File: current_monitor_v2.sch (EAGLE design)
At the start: 21 parts, among them IC1 LT1495, J1 1X2-3.5MM, J2 1X2-3.5MM, SW2 Display, T1 2N3904, T2 2N3904, U1 ARDUINO_SHIELDLABEL

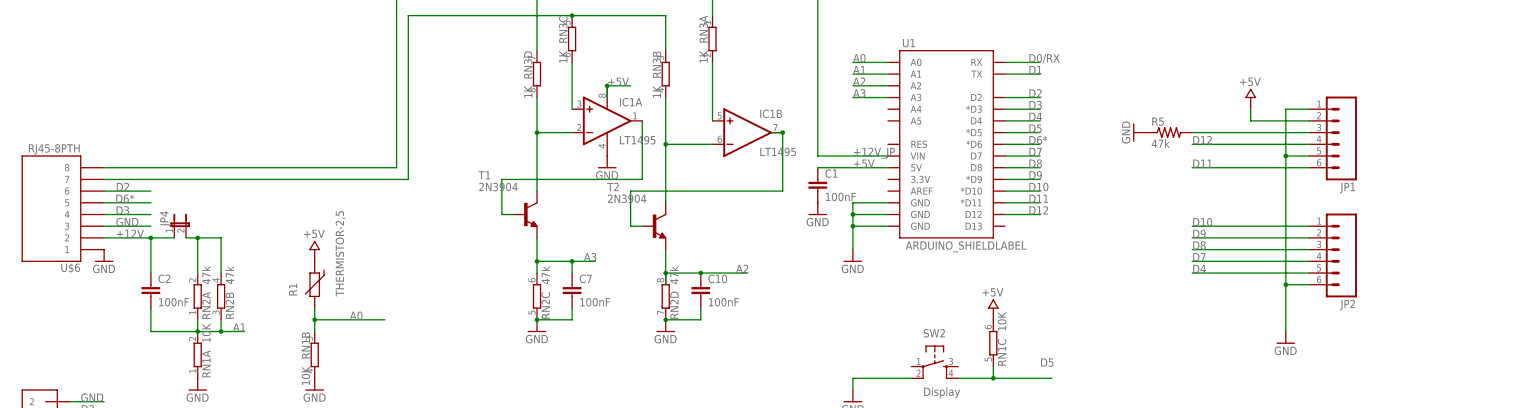
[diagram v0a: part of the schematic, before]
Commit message: changed v1.1 to v1-1 to please git, surface mount board ready to submit to osh park
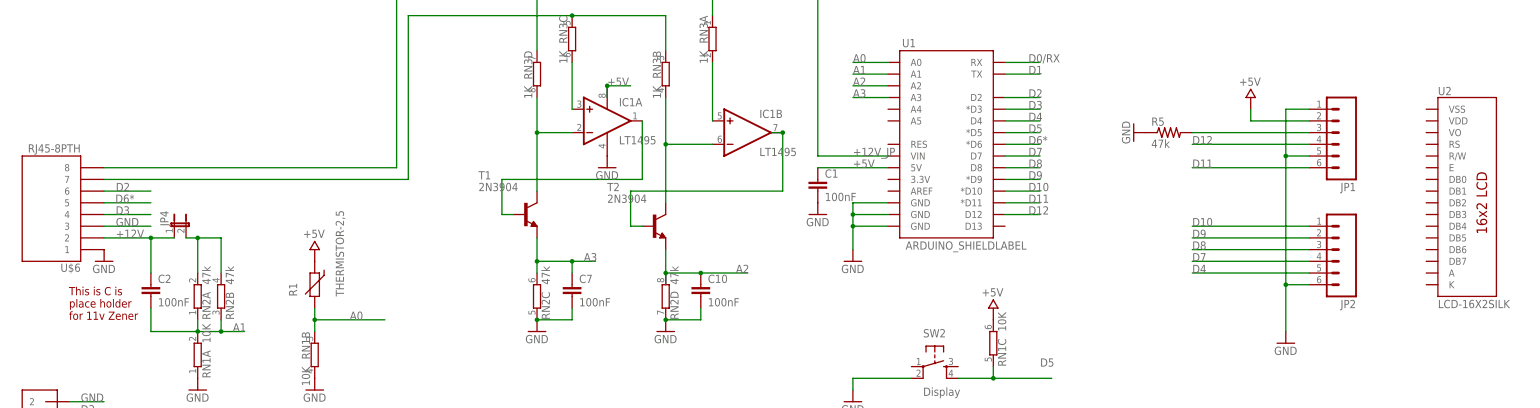
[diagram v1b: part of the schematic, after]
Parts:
- added U2: LCD-16X2SILK, SparkFun-Displays:LCD-16X2SILK
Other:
- note added: "This is C is place holder for 11v Zener"
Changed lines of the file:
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@@
 <part name="JP3" library="SparkFun-Passives" deviceset="JUMPER-2" device="PTH"/>
 <part name="JP4" library="SparkFun-Passives" deviceset="JUMPER-2" device="PTH"/>
+<part name="U2" library="SparkFun-Displays" deviceset="LCD-16X2" device="SILK"/>
 </parts>
 <sheets>
@@
 <text x="189.23" y="-58.928" size="2.54" layer="97">8</text>
 <text x="190.5" y="-68.58" size="1.778" layer="91">GJH</text>
+<text x="-106.68" y="53.34" size="1.778" layer="94">This is C is
+place holder
+for 11v Zener</text>
 </plain>
 <instances>
@@
 <instance part="JP3" gate="A" x="48.26" y="132.08"/>
 <instance part="JP4" gate="A" x="-83.82" y="73.66"/>
+<instance part="U2" gate="G$1" x="198.12" y="78.74"/>
 </instances>
 <busses>
@@
 </schematic>
 </drawing>
+<compatibility>
+<note version="6.3" minversion="6.2.2" severity="warning">
+Since Version 6.2.2 text objects can contain more than one line,
+which will not be processed correctly with this version.
+</note>
+</compatibility>
 </eagle>
